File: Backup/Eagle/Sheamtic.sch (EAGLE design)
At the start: 15 parts, among them IC1 PIC16F874P

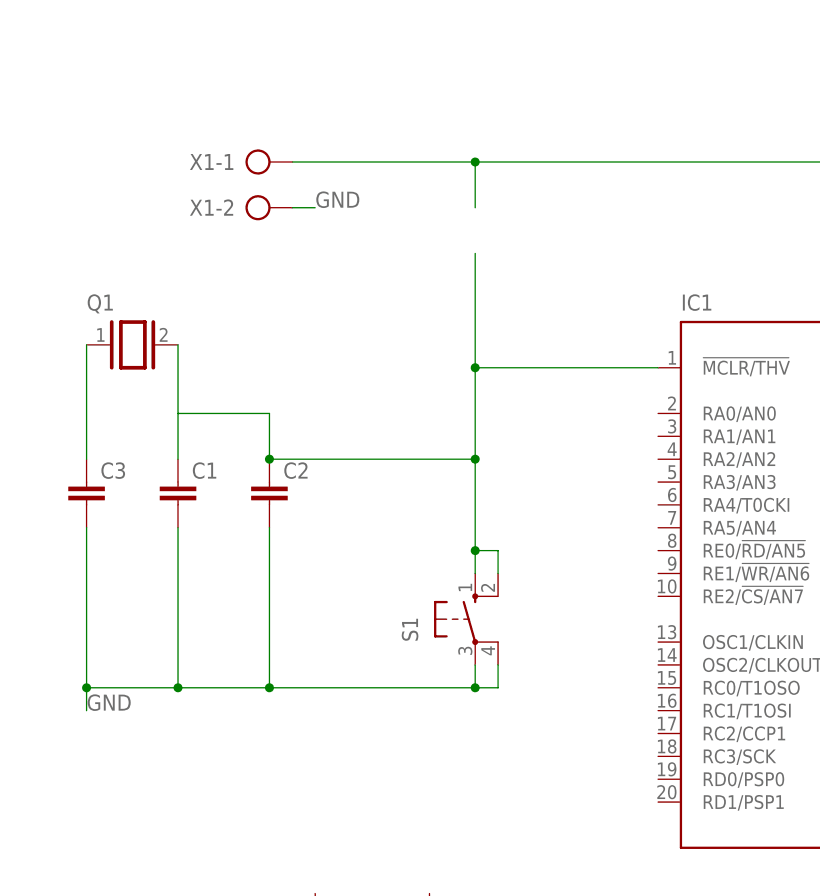
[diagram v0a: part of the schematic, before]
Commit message: correction proteus/eagle + test pic ccs
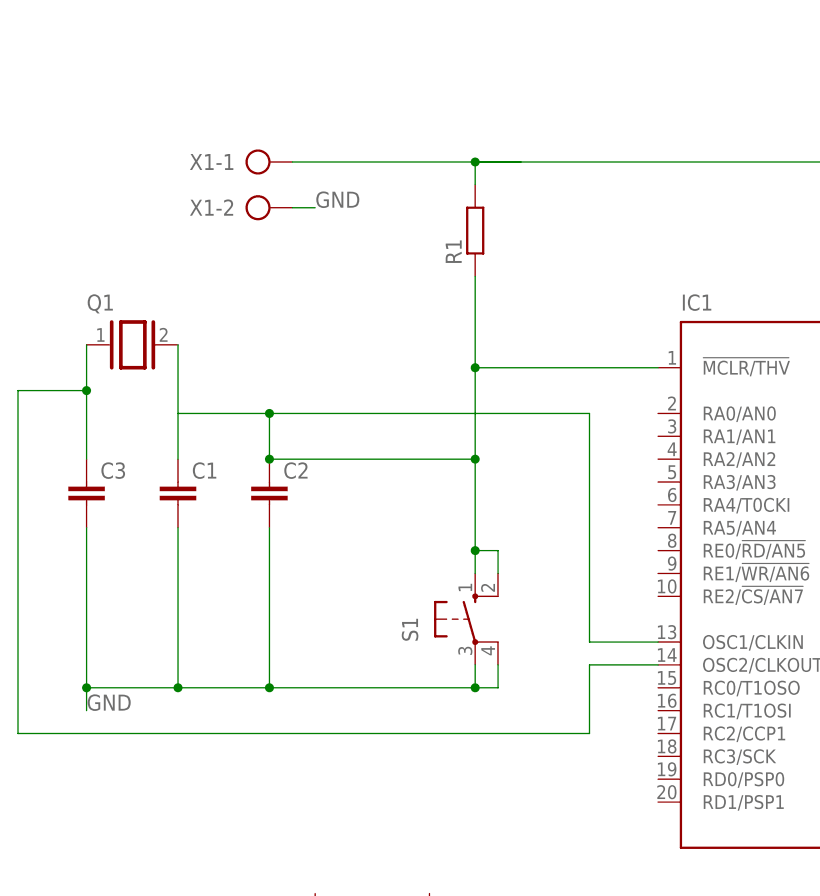
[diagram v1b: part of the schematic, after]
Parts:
- added R1: (no value), rcl:R-EU_0204/7
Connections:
- net N$1: now also R1.2
- net N$2: now also IC1.OSC1/CLKIN, R1.1
- net N$5: now also IC1.OSC2/CLKOUT
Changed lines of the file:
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@@
 <part name="Q1" library="special" library_urn="urn:adsk.eagle:library:367" deviceset="XTAL/S" device="" package3d_urn="urn:adsk.eagle:package:26647/2"/>
 <part name="LED2" library="led" library_urn="urn:adsk.eagle:library:259" deviceset="LED" device="5MM" package3d_urn="urn:adsk.eagle:package:15799/2"/>
+<part name="R1" library="rcl" library_urn="urn:adsk.eagle:library:334" deviceset="R-EU_" device="0204/7" package3d_urn="urn:adsk.eagle:package:23498/2"/>
 </parts>
 <sheets>
@@
 <attribute name="VALUE" x="31.115" y="-7.112" size="1.778" layer="96" rot="R90"/>
 </instance>
+<instance part="R1" gate="G$1" x="30.48" y="73.66" smashed="yes" rot="R90">
+<attribute name="NAME" x="28.9814" y="69.85" size="1.778" layer="95" rot="R90"/>
+<attribute name="VALUE" x="33.782" y="69.85" size="1.778" layer="96" rot="R90"/>
+</instance>
 </instances>
 <busses>
@@
 <wire x1="71.12" y1="68.58" x2="73.66" y2="68.58" width="0.1524" layer="91"/>
 <junction x="73.66" y="68.58"/>
-<wire x1="30.48" y1="81.28" x2="30.48" y2="76.2" width="0.1524" layer="91"/>
+<wire x1="30.48" y1="81.28" x2="35.56" y2="81.28" width="0.1524" layer="91"/>
 <junction x="30.48" y="81.28"/>
+<pinref part="R1" gate="G$1" pin="2"/>
+<wire x1="30.48" y1="78.74" x2="30.48" y2="81.28" width="0.1524" layer="91"/>
 </segment>
 </net>
@@
 <junction x="7.62" y="48.26"/>
 <wire x1="7.62" y1="53.34" x2="-2.54" y2="53.34" width="0.1524" layer="91"/>
-<wire x1="30.48" y1="58.42" x2="30.48" y2="71.12" width="0.1524" layer="91"/>
 <junction x="30.48" y="58.42"/>
+<wire x1="7.62" y1="53.34" x2="43.18" y2="53.34" width="0.1524" layer="91"/>
+<wire x1="43.18" y1="53.34" x2="43.18" y2="27.94" width="0.1524" layer="91"/>
+<junction x="7.62" y="53.34"/>
+<pinref part="IC1" gate="G$1" pin="OSC1/CLKIN"/>
+<wire x1="43.18" y1="27.94" x2="50.8" y2="27.94" width="0.1524" layer="91"/>
+<pinref part="R1" gate="G$1" pin="1"/>
+<wire x1="30.48" y1="58.42" x2="30.48" y2="68.58" width="0.1524" layer="91"/>
 </segment>
 </net>
@@
 <pinref part="C3" gate="G$1" pin="1"/>
 <pinref part="Q1" gate="G$1" pin="1"/>
-<wire x1="-12.7" y1="60.96" x2="-12.7" y2="48.26" width="0.1524" layer="91"/>
+<wire x1="-12.7" y1="60.96" x2="-12.7" y2="55.88" width="0.1524" layer="91"/>
+<pinref part="IC1" gate="G$1" pin="OSC2/CLKOUT"/>
+<wire x1="-12.7" y1="55.88" x2="-12.7" y2="48.26" width="0.1524" layer="91"/>
+<wire x1="50.8" y1="25.4" x2="43.18" y2="25.4" width="0.1524" layer="91"/>
+<wire x1="43.18" y1="25.4" x2="43.18" y2="17.78" width="0.1524" layer="91"/>
+<wire x1="43.18" y1="17.78" x2="-20.32" y2="17.78" width="0.1524" layer="91"/>
+<wire x1="-20.32" y1="17.78" x2="-20.32" y2="55.88" width="0.1524" layer="91"/>
+<wire x1="-20.32" y1="55.88" x2="-12.7" y2="55.88" width="0.1524" layer="91"/>
+<junction x="-12.7" y="55.88"/>
 </segment>
 </net>
